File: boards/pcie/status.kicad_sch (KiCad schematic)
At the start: 11 parts, among them J3 12V, J4 5V, J5 3V3, J6 1V0, J7 GND

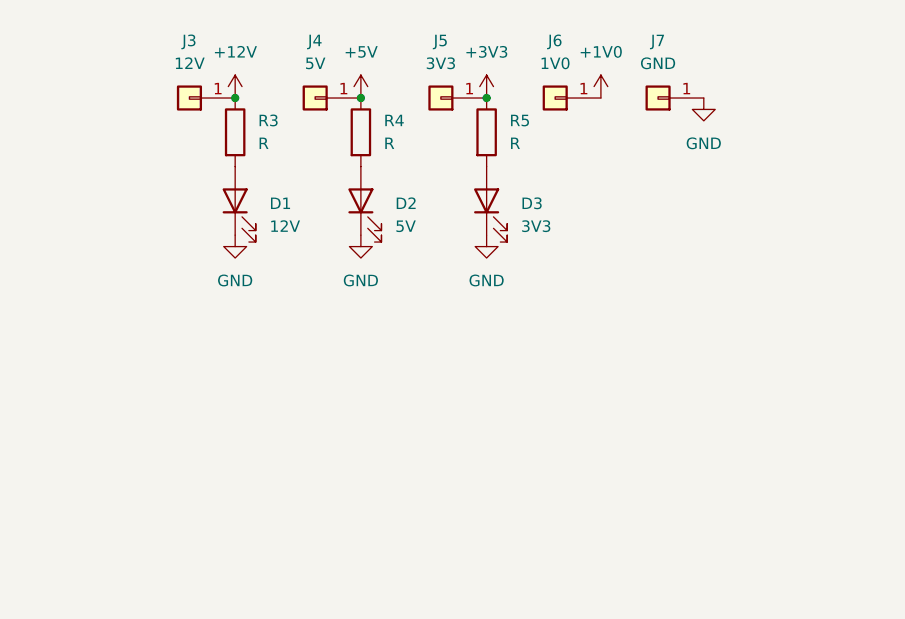
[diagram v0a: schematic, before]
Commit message: pcie: add leds, buck regulators
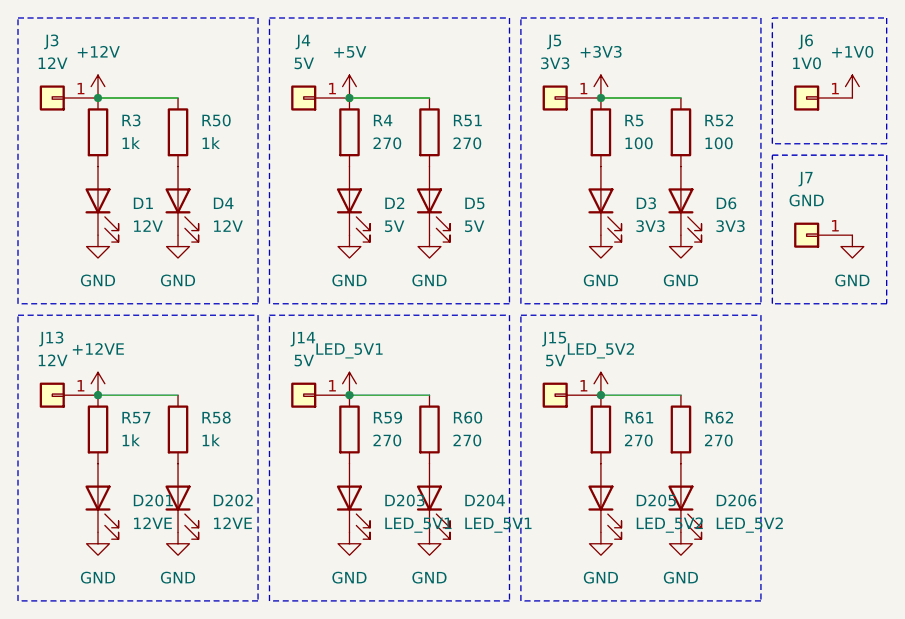
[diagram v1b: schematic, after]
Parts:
- added D201, D202: 12VE, LED_SMD:LED_1206_3216Metric, symbol Device:LED
- added D203, D204: LED_5V1, LED_SMD:LED_1206_3216Metric, symbol Device:LED
- added D205, D206: LED_5V2, LED_SMD:LED_1206_3216Metric, symbol Device:LED
- added D4: 12V, LED_SMD:LED_1206_3216Metric, symbol Device:LED
- added D5: 5V, LED_SMD:LED_1206_3216Metric, symbol Device:LED
- added D6: 3V3, LED_SMD:LED_1206_3216Metric, symbol Device:LED
- added J13: 12V, Connector_PinHeader_2.54mm:PinHeader_1x01_P2.54mm_Vertical, symbol Connector_Generic:Conn_01x01
- added J14, J15: 5V, Connector_PinHeader_2.54mm:PinHeader_1x01_P2.54mm_Vertical, symbol Connector_Generic:Conn_01x01
- added R50, R57, R58: 1k, Resistor_SMD:R_0402_1005Metric, symbol Device:R
- added R51, R59, R60, R61, R62: 270, Resistor_SMD:R_0402_1005Metric, symbol Device:R
- added R52: 100, Resistor_SMD:R_0402_1005Metric, symbol Device:R
- D1, D2, D3: LCSC (none) -> C965823
- R3: value R -> 1k
- R4: value R -> 270
- R5: value R -> 100
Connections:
- net +12V: now also R50.1
- net +3V3: now also R52.1
- net +5V: now also R51.1
- net GND: now also D201.1 (K), D202.1 (K), D203.1 (K), D204.1 (K), D205.1 (K), D206.1 (K), D4.1 (K), D5.1 (K), D6.1 (K)
- new net: D203.2 (A), R59.2
- new net: D204.2 (A), R60.2
- new net: D4.2 (A), R50.2
- new net: D202.2 (A), R58.2
- new net: D5.2 (A), R51.2
- new net: D206.2 (A), R62.2
- new net: D6.2 (A), R52.2
- new net: D205.2 (A), R61.2
- new net: D201.2 (A), R57.2
- new net +12VE: J13.1 (Pin_1), R57.1, R58.1
- new net LED_5V1: J14.1 (Pin_1), R59.1, R60.1
- new net LED_5V2: J15.1 (Pin_1), R61.1, R62.1
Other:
- moved on the sheet: D1, D2, D3, J3, J4, J5, J6, J7, R3, R4, R5
